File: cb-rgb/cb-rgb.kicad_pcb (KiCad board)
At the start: 4 copper layers, 25.4 x 55.8 mm, 18 parts, among them P1 CONN_01X14, P2 CONN_01X14, P3 CONN_8, Q1 MOS_N, Q2 MOS_N, Q3 MOS_N, U2 UA78M33

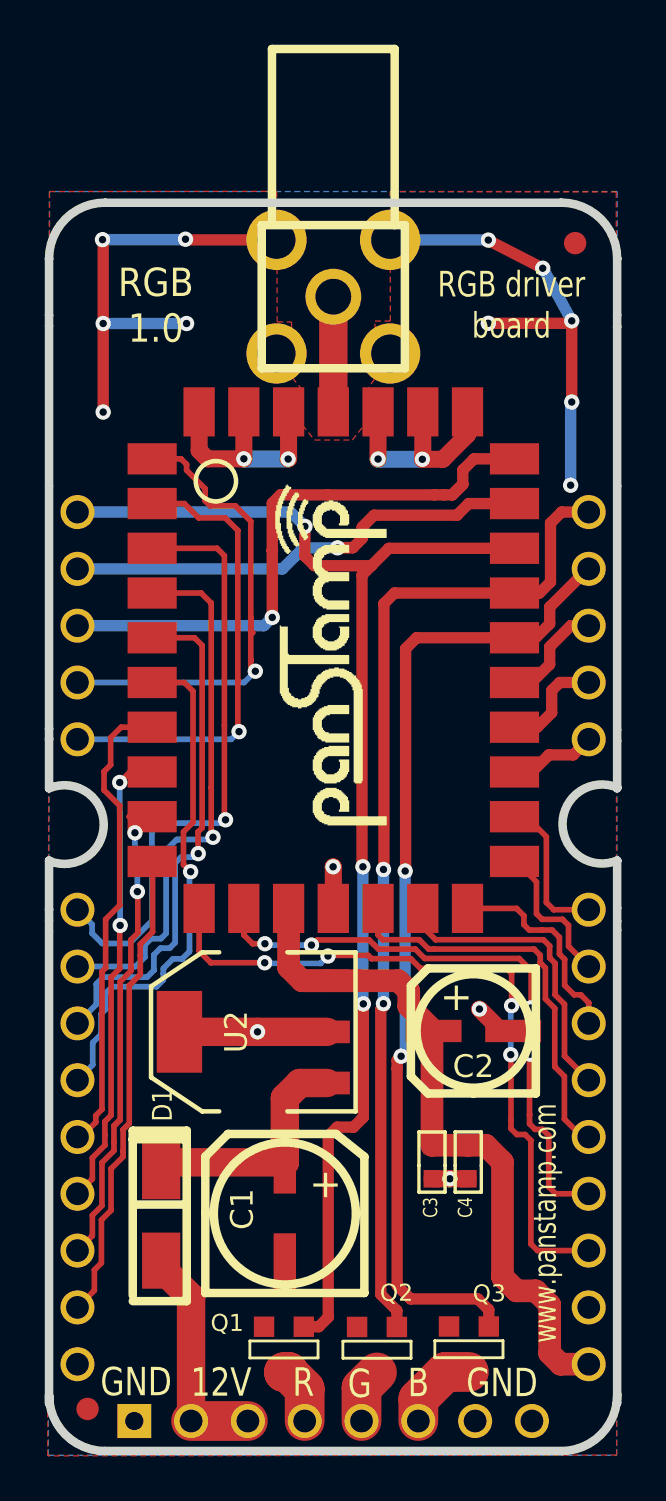
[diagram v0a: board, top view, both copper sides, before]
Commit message: PWM pins fixed
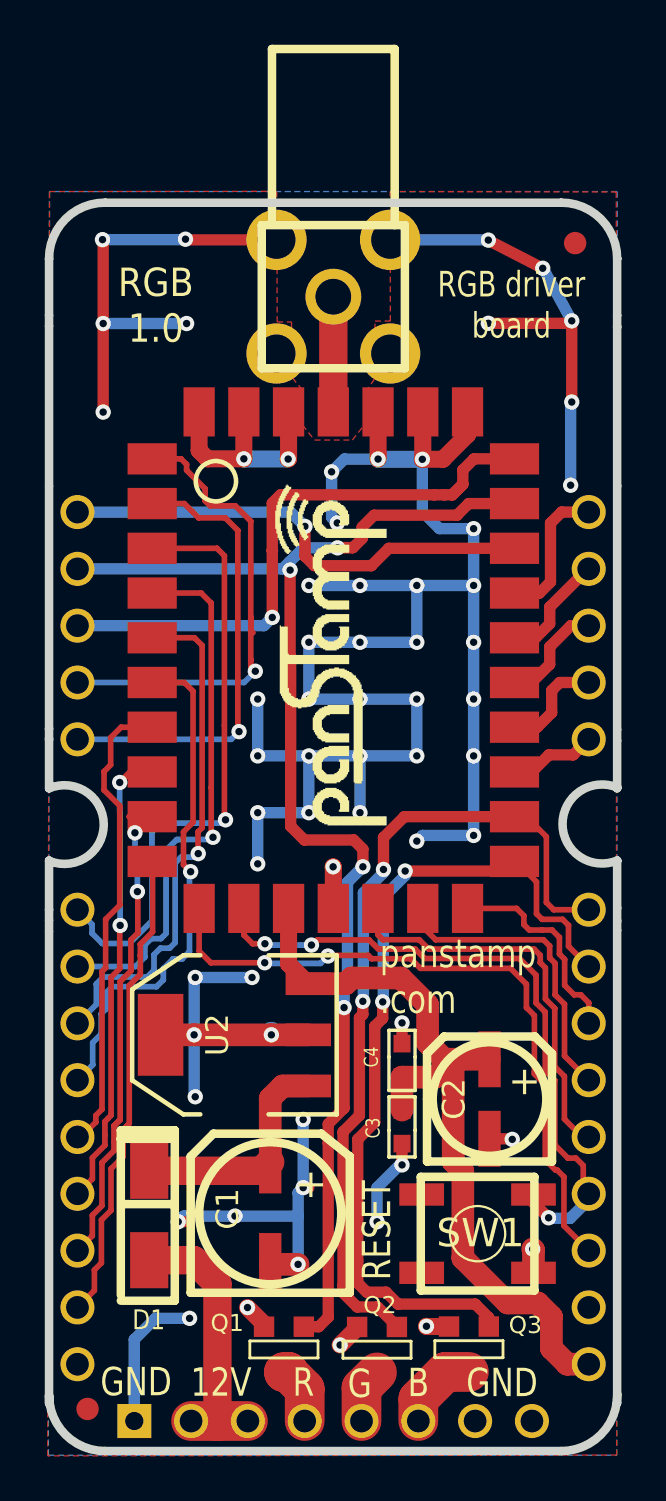
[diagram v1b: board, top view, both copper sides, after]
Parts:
- added SW1: SW_PUSH, mysmd:switch-tact-noah, F.Cu at (136.1, 117.4)
- moved C4 5.42 mm to (132.7, 109.6), turned to 90 degrees
- moved C2 3.13 mm to (136.6, 111.4), turned to 270 degrees
- moved C3 2.07 mm to (132.7, 112.6)
- moved U2 0.85 mm to (125.2, 108.5)
- moved C1 0.65 mm to (126.8, 116.5)
- moved D1 0.53 mm to (121.4, 116.6)
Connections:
- P2 pad 2: /BLUE_CH -> /D22
- P2 pad 7: /D4 -> /BLUE_CH
- PS1 pad 18: /D4 -> /BLUE_CH
- PS1 pad 23: /BLUE_CH -> /D22
- Q1 pad G: /D20 -> /D19
- Q2 pad G: /D21 -> /D3
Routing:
- net GND: track 72.4 -> 177.5 mm, vias 19 -> 62
- net /D21: track 45.1 -> 6.36 mm, vias 2 -> 0
- net /D19: track 22.4 -> 60.8 mm, vias 1 -> 4
- net /D20: track 57.8 -> 21.7 mm, vias 3 -> 1
- net /D3: track 7.07 -> 37.5 mm, vias 0 -> 2
- net /D4: track 7.18 -> 0.00 mm
- net /BLUE_CH: track 44.3 -> 38.5 mm
- net /D22: track 0.00 -> 5.25 mm
- net VCC: track 31.2 -> 36.0 mm
- net /RESET: track 27.9 -> 30.7 mm, vias 4 -> 3
- net /TEST: track 33.9 -> 31.4 mm, vias 4 -> 2
- net +12V: track 10.3 -> 12.2 mm
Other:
- board text added: "panstamp .com"

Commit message: Version changed
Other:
- board text added: "RGB 2.0"
- board text removed: "RGB 1.0"
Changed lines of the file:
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@@
-(kicad_pcb (version 4) (host pcbnew 0.201512201246+6385~39~ubuntu14.04.1-stable)
+(kicad_pcb (version 4) (host pcbnew 0.201601211448+6504~42~ubuntu14.04.1-product)
   (general
     (links 67)
     (no_connects 0)
-    (area 116.717219 71.084879 142.508661 127.283401)
+    (area 113.793486 64.063159 145.991514 132.5316)
     (thickness 1.6002)
     (drawings 83)
@@
   (page A4)
   (title_block
-    (title "USB carrier board for panStamp, aka panStick")
-    (date "25 Feb 2015")
-    (rev 4.0)
-    (company panStamp)
+    (title "RGB driver board for panStamp")
+    (date 2016-01-22)
+    (rev 2.0)
+    (company www.panstamp.com)
   )
   (layers
@@
   )
   (setup
-    (last_trace_width 0.508)
+    (last_trace_width 0.1524)
     (user_trace_width 0.2032)
     (user_trace_width 0.254)
@@
     (visible_elements FFFFF7BF)
     (pcbplotparams
-      (layerselection 0x010f0_80000001)
+      (layerselection 0x010f0_fffffff9)
       (usegerberextensions true)
       (excludeedgelayer true)
@@
   (gr_line (start 142.30772 124.51008) (end 142.30772 103.82008) (angle 90) (layer Edge.Cuts) (width 0.381))
   (gr_line (start 116.90772 103.88008) (end 116.90772 124.98008) (angle 90) (layer Edge.Cuts) (width 0.381))
-  (gr_text "RGB\n1.0" (at 121.68 75.885) (layer F.SilkS)
+  (gr_text "RGB\n2.0" (at 121.68 75.885) (layer F.SilkS)
     (effects (font (size 1.27 1.143) (thickness 0.1524)))
   )
